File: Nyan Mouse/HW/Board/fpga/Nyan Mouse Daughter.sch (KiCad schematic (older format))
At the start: 30 parts

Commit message: Finalized connector structure.
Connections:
- net labels added: gyro_a, re1, re2, re3, re4, re5, re6
- wire segments 125 -> 138
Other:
- moved on the sheet: P?
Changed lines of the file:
@@
 LIBS:contrib
 LIBS:valves
-LIBS:drv8837
-LIBS:s25fl064p
-LIBS:mic94345-4ycs
-LIBS:lp3987
-LIBS:altera_ep4ce15e22c
-LIBS:3v3custom
-LIBS:tps6205x
-LIBS:stm32f103rx
-LIBS:SparkFun
-LIBS:JST-XH-BattBalance
 LIBS:Nyan Mouse Daughter-cache
 EELAYER 24 0
@@
 L CONN_20X2 P?
 U 1 1 5358CF36
-P 4450 5050
-F 0 "P?" H 4450 6100 60  0000 C CNN
-F 1 "CONN_20X2" V 4450 5050 50  0000 C CNN
-F 2 "" H 4450 5050 60  0000 C CNN
-F 3 "" H 4450 5050 60  0000 C CNN
-	1    4450 5050
-	1    0    0    -1
-$EndComp
+P 3300 5650
+F 0 "P?" H 3300 6700 60  0000 C CNN
+F 1 "CONN_20X2" V 3300 5650 50  0000 C CNN
+F 2 "" H 3300 5650 60  0000 C CNN
+F 3 "" H 3300 5650 60  0000 C CNN
+	1    3300 5650
+	1    0    0    -1
+$EndComp
+$Comp
+L AGND #PWR?
+U 1 1 5358CD8B
+P 2750 6600
+F 0 "#PWR?" H 2750 6600 40  0001 C CNN
+F 1 "AGND" V 2750 6450 50  0000 C CNN
+F 2 "" H 2750 6600 60  0000 C CNN
+F 3 "" H 2750 6600 60  0000 C CNN
+	1    2750 6600
+	0    1    1    0
+$EndComp
+$Comp
+L AGND #PWR?
+U 1 1 5358CD9D
+P 2750 5800
+F 0 "#PWR?" H 2750 5800 40  0001 C CNN
+F 1 "AGND" V 2750 5650 50  0000 C CNN
+F 2 "" H 2750 5800 60  0000 C CNN
+F 3 "" H 2750 5800 60  0000 C CNN
+	1    2750 5800
+	0    1    1    0
+$EndComp
+Wire Wire Line
+	2750 6600 2900 6600
+Wire Wire Line
+	2900 5800 2750 5800
+Wire Wire Line
+	2900 6000 2550 6000
+Wire Wire Line
+	2900 6100 2550 6100
+Wire Wire Line
+	2900 6200 2550 6200
+Wire Wire Line
+	2900 6300 2550 6300
+Wire Wire Line
+	2900 6400 2550 6400
+Wire Wire Line
+	2900 6500 2550 6500
+Wire Wire Line
+	2900 5900 2550 5900
+Text Label 2600 5900 0    60   ~ 0
+re1
+Text Label 2600 6000 0    60   ~ 0
+re2
+Text Label 2600 6100 0    60   ~ 0
+re3
+Text Label 2600 6200 0    60   ~ 0
+re4
+Text Label 2600 6300 0    60   ~ 0
+re5
+Text Label 2600 6400 0    60   ~ 0
+re6
+Text Label 2600 6500 0    60   ~ 0
+gyro_a
+Wire Wire Line
+	2900 4900 2850 4900
+Wire Wire Line
+	2850 4900 2850 4650
+$Comp
+L DGND #PWR?
+U 1 1 5358D30B
+P 2850 4650
+F 0 "#PWR?" H 2850 4650 40  0001 C CNN
+F 1 "DGND" H 2850 4580 40  0000 C CNN
+F 2 "" H 2850 4650 60  0000 C CNN
+F 3 "" H 2850 4650 60  0000 C CNN
+	1    2850 4650
+	-1   0    0    1
+$EndComp
+Wire Wire Line
+	2900 4700 2850 4700
+Connection ~ 2850 4700
+Wire Wire Line
+	2850 4800 2900 4800
+Connection ~ 2850 4800
 $EndSCHEMATC

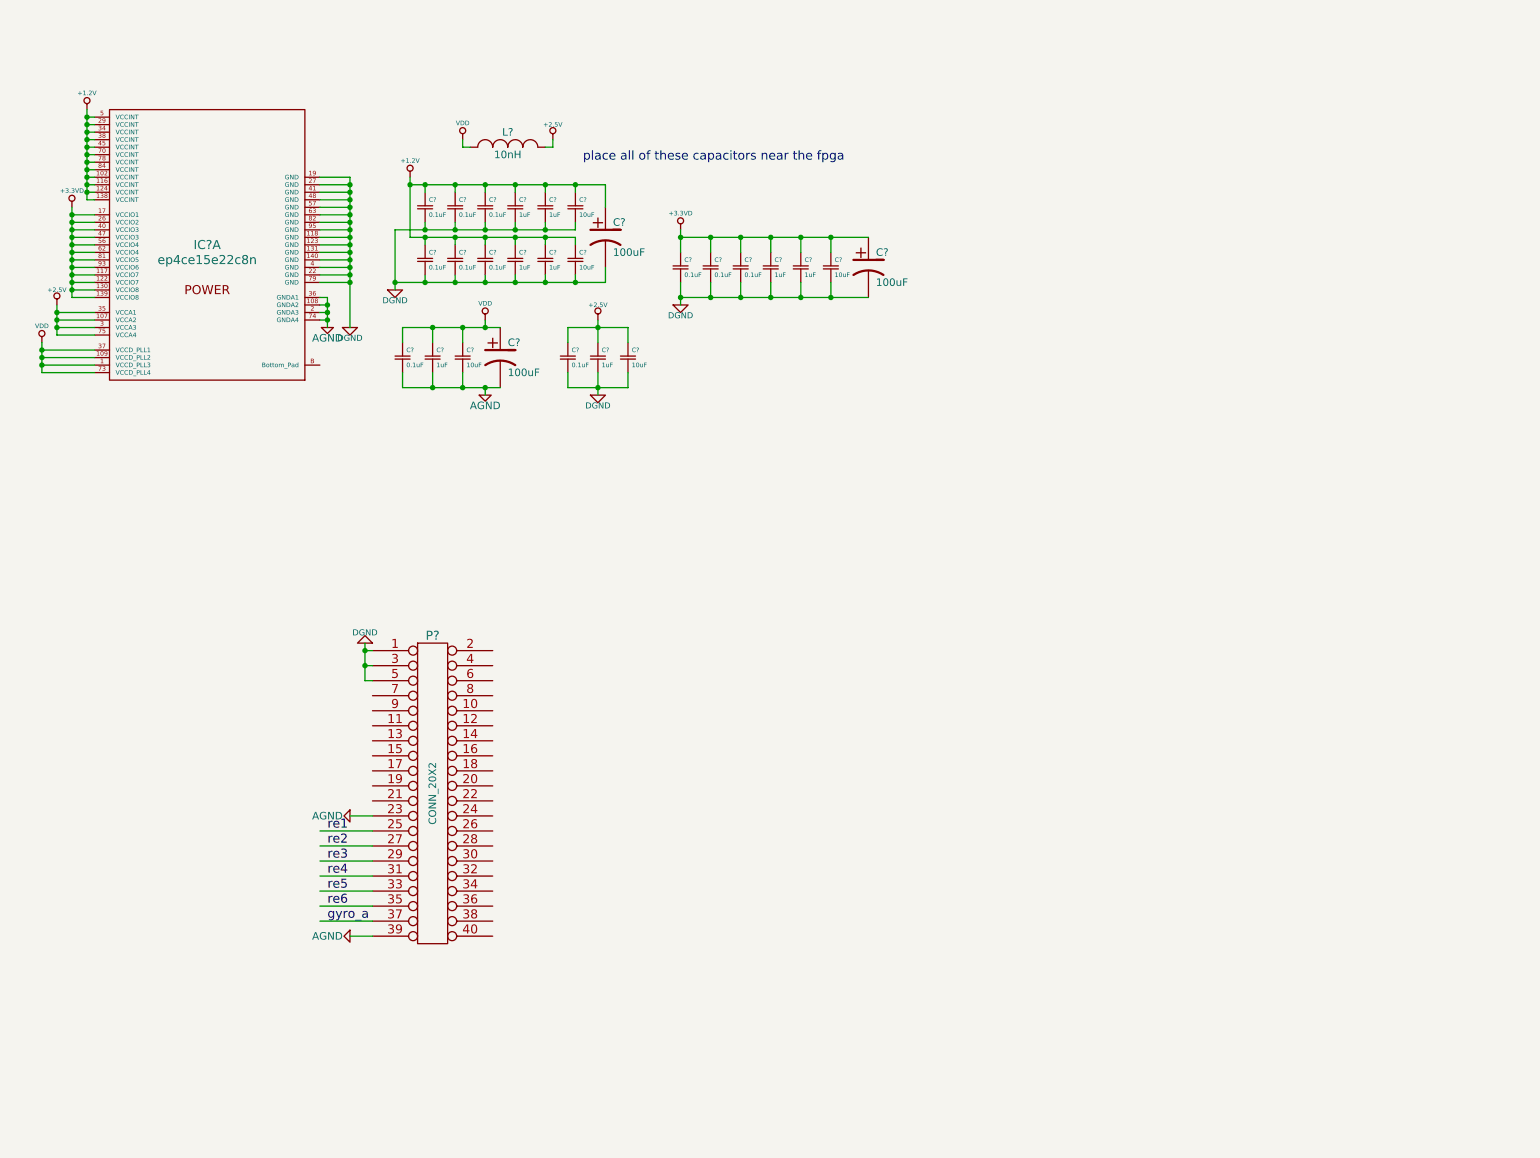
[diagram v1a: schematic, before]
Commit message: Repopulated FPGA portions...
Where did my changes go?
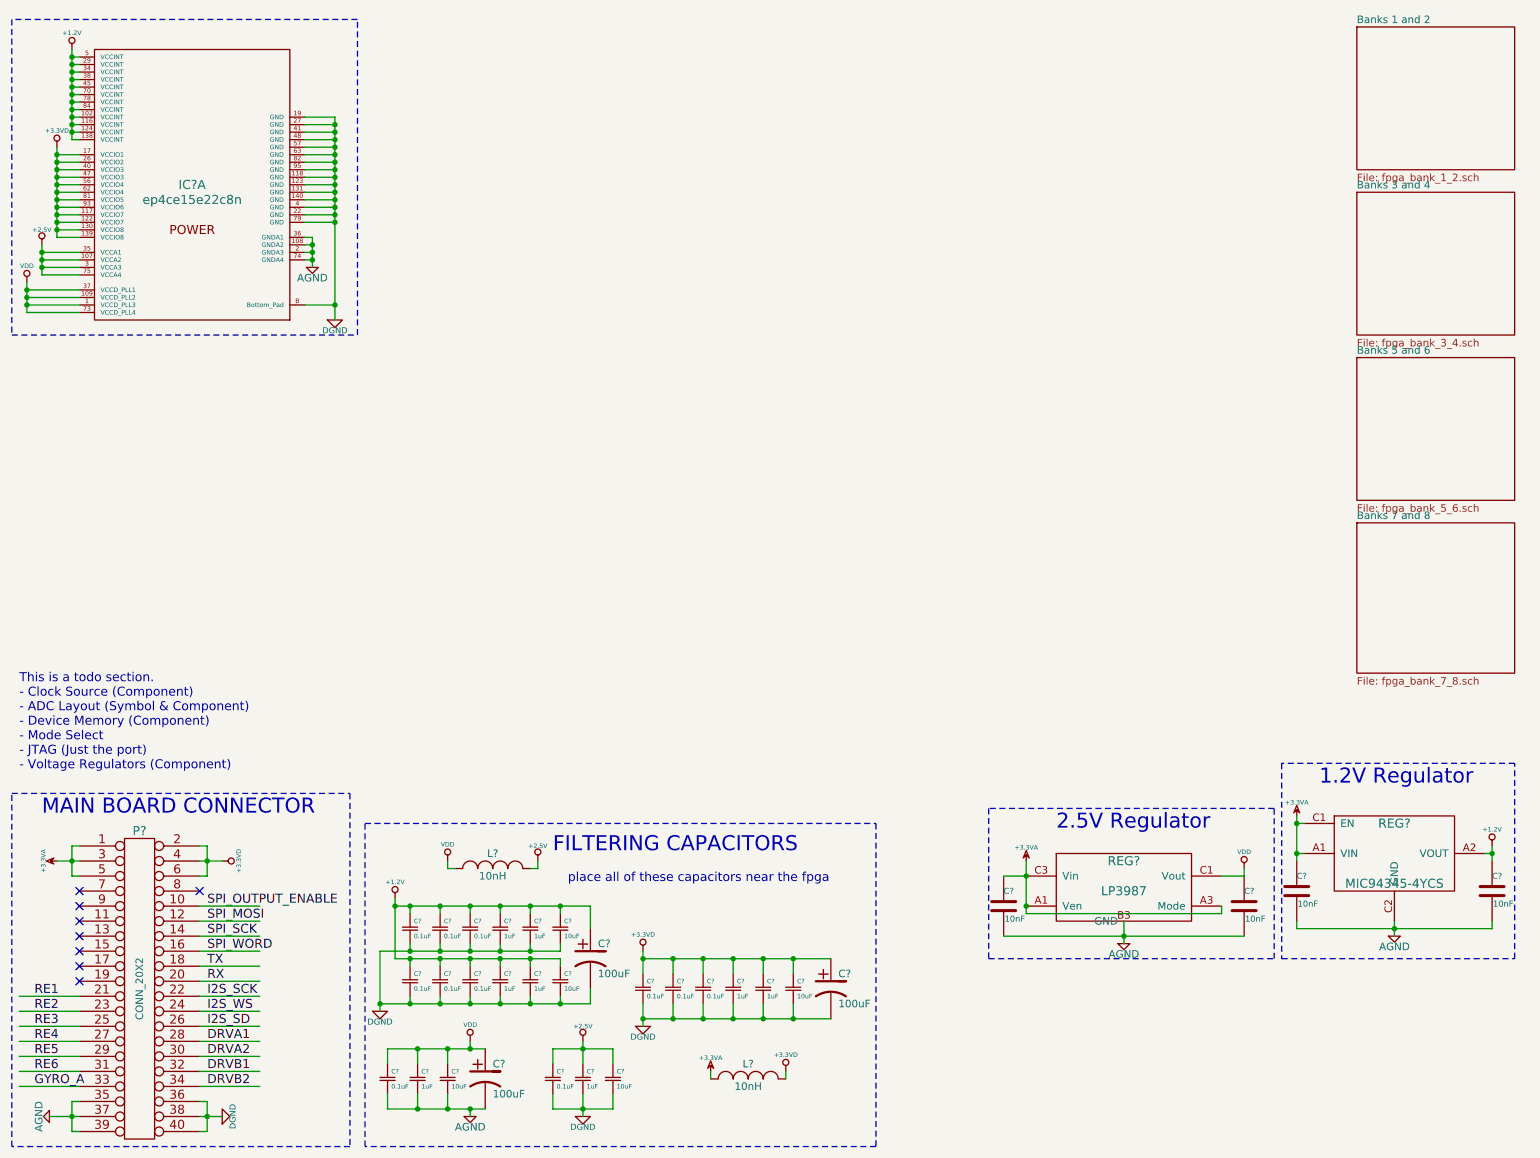
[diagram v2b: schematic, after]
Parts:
- added C? (x4): 10nF, symbol C
- added L?: 10nH, symbol INDUCTOR_SMALL
- added REG?: LP3987, symbol LP3987
- added REG?: MIC94345-4YCS, symbol MIC94345-4YCS
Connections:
- net labels added: +3.3VA, DRVA1, DRVA2, DRVB1, DRVB2, GYRO_A, I2S_SCK, I2S_SD, I2S_WS, RE1, RE2, RE3, RE4, RE5, RE6, RX, SPI_MOSI, SPI_OUTPUT_ENABLE, SPI_SCK, SPI_WORD, TX
- net labels removed: gyro_a, re1, re2, re3, re4, re5, re6
- wire segments 138 -> 181
- no-connect marks 0 -> 8
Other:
- note added: "1.2V Regulator"
- note added: "2.5V Regulator"
- note added: "FILTERING CAPACITORS"
- note added: "MAIN BOARD CONNECTOR"
- note added: "This is a todo section.\n- Clock Source (Component)\n- ADC Layout (Symbol & Component)\n- Device Memory (Component)\n- Mode Select\n- JTAG (Just the port)\n- Voltage Regulators (Component)"
- moved on the sheet: C?, IC?A, L?, P?

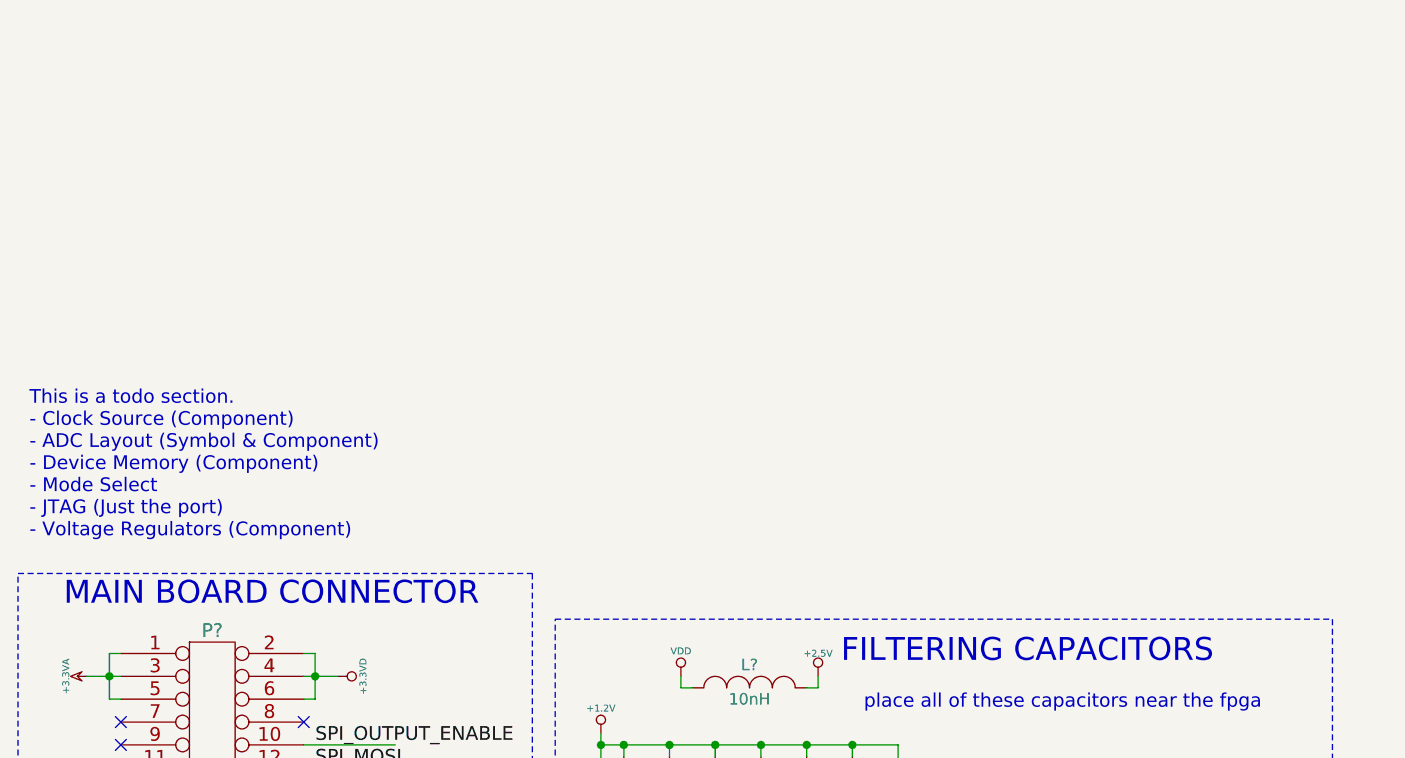
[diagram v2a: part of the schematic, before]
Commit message: Added ESD prevention documentation.
Added ByteBlaster documentation.

Modified FPGA banks.
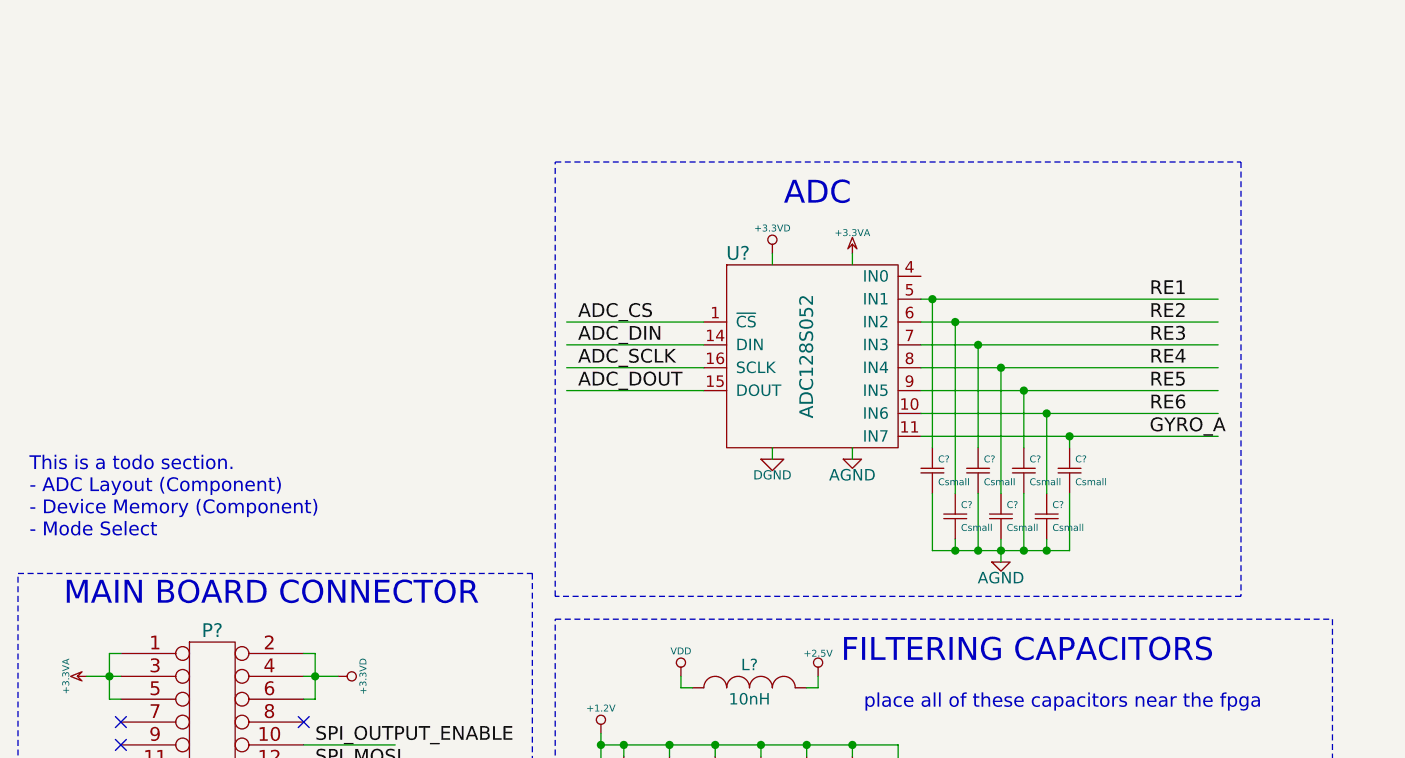
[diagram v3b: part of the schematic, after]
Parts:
- added C? (x7): Csmall, symbol Csmall
- added U?: ADC128S052, symbol ADC128S052
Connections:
- net labels added: ADC_CS, ADC_DIN, ADC_DOUT, ADC_SCLK
- wire segments 181 -> 211
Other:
- note added: "ADC"
- note added: "This is a todo section.\n- ADC Layout (Component)\n- Device Memory (Component)\n- Mode Select"
- note removed: "This is a todo section.\n- Clock Source (Component)\n- ADC Layout (Symbol & Component)\n- Device Memory (Component)\n- Mode Select\n- JTAG (Just the port)\n- Voltage Regulators (Component)"
